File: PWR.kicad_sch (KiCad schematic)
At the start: 36 parts, among them J1 Conn_01x04_Pin, J10 Conn_01x02_Pin, J2 Conn_01x03_Pin, J3 Conn_01x03_Pin, J4 Conn_01x03_Pin, J5 Conn_01x03_Pin, U1 LM66100DCK, U2 XC6206P332MR, U4 MCP6001-OT

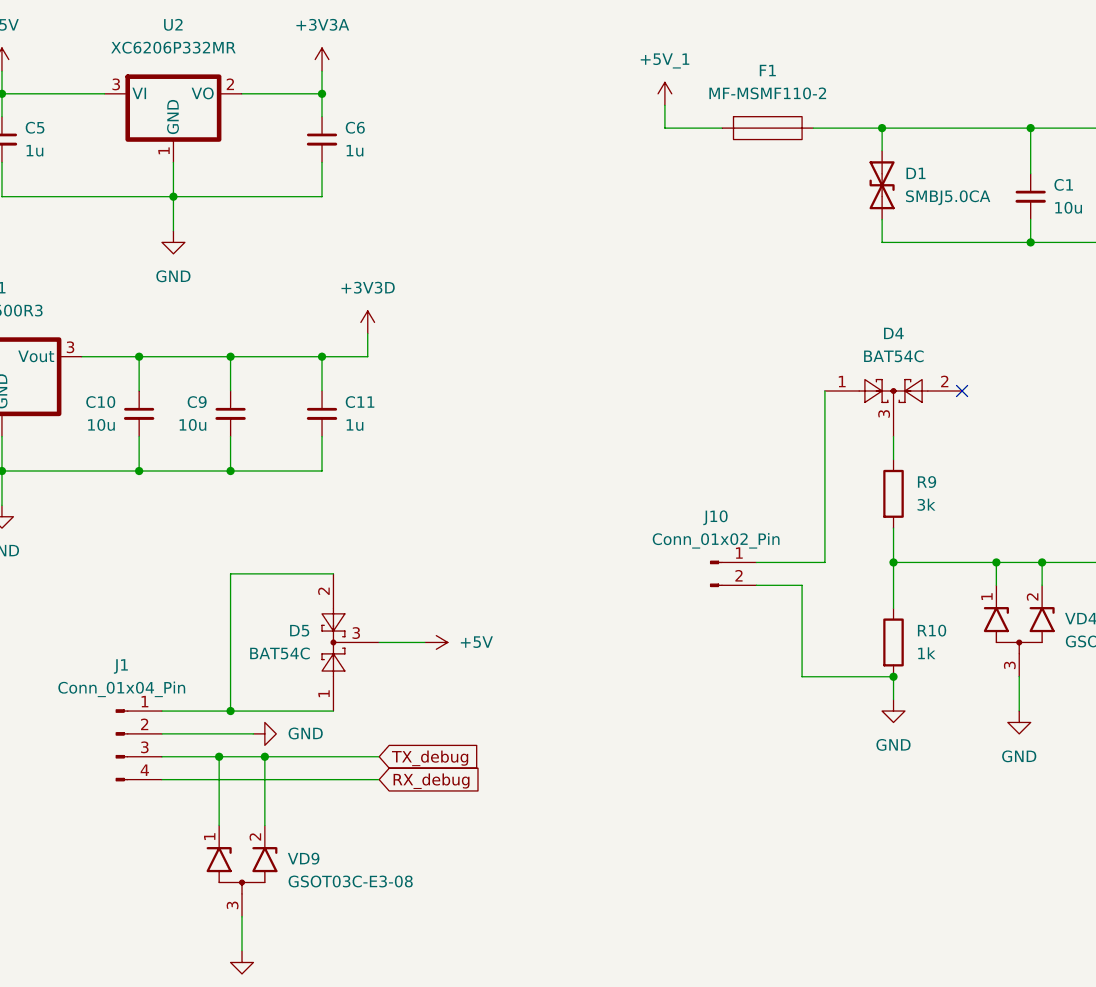
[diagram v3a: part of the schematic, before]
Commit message: feat: complete schematic, and start PCB
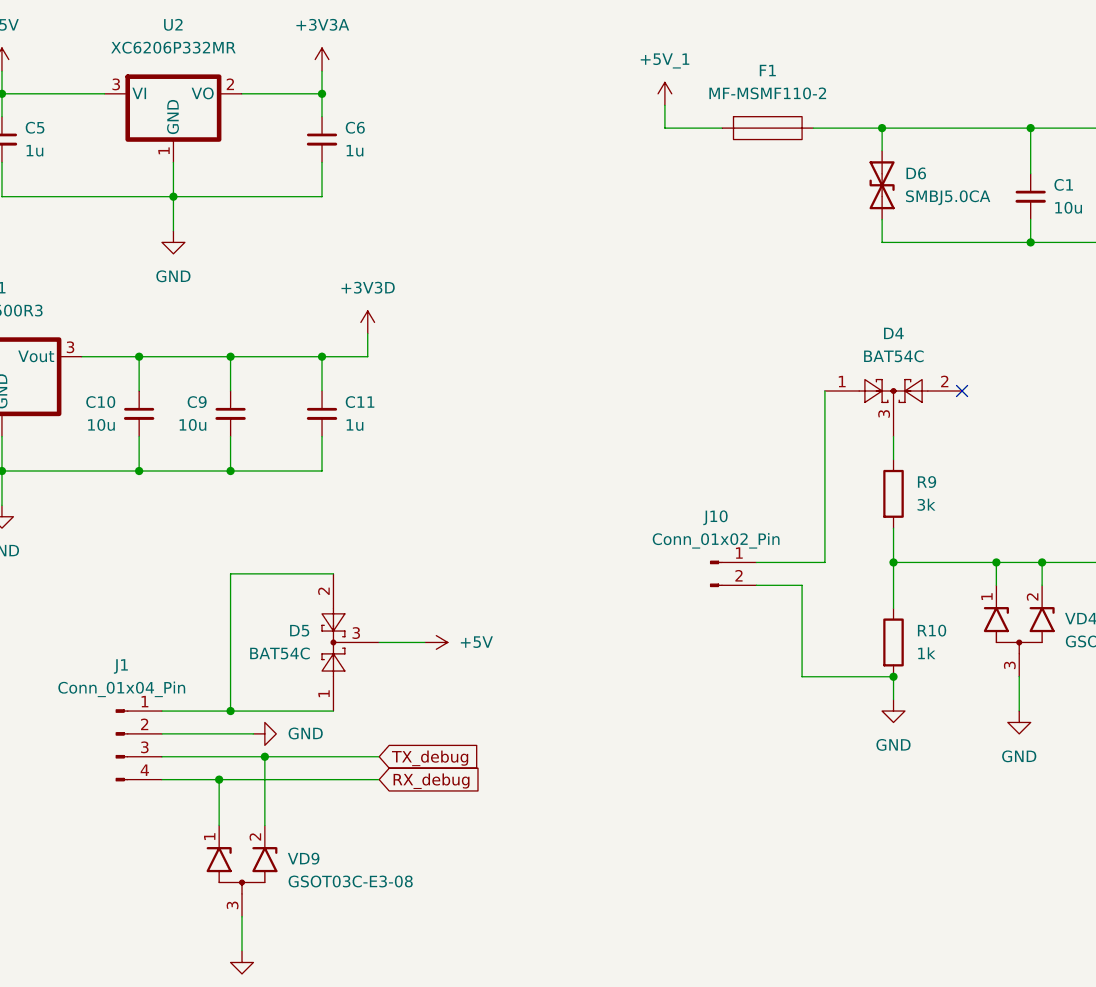
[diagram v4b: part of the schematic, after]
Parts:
- removed D1: SMBJ5.0CA, Diode_SMD:D_SMB_Handsoldering, symbol TVS:SMBJ5.0CA
- added D6: SMBJ5.0CA, Diode_SMD:D_SMB_Handsoldering, symbol TVS:SMBJ5.0CA
- C10, C11, C2, C3, C4, C5, C6, C7, C8, C9: footprint Capacitor_SMD:C_0805_2012Metric -> Capacitor_SMD:C_0805_2012Metric_Pad1.18x1.45mm_HandSolder
- U2: footprint Package_TO_SOT_SMD:SOT-23-3 -> Package_TO_SOT_SMD:SOT-23_Handsoldering
- U4: footprint Package_TO_SOT_SMD:SOT-23-5 -> Package_TO_SOT_SMD:SOT-23-5_HandSoldering
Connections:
- net +5V_1: now also F1.1 (A1); no longer F1.
- net GND: now also D6.1 (A1)
- net RX_debug: now also VD9.1 (K1)
- net TX_debug: no longer VD9.1 (K1)
- net at C1.1, C2.1, C3.1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: now also F1.2 (A2), D6.2 (A2); no longer F1.
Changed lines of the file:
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@@
 	)
 	(junction
+		(at 85.09 153.67)
+		(diameter 0)
+		(color 0 0 0 0)
+	)
+	(junction
 		(at 140.97 40.64)
 		(diameter 0)
@@
 	)
 	(junction
-		(at 85.09 151.13)
-		(diameter 0)
-		(color 0 0 0 0)
-	)
-	(junction
 		(at 199.39 129.54)
 		(diameter 0)
@@
 	(wire
 		(pts
-			(xy 85.09 151.13) (xy 90.17 151.13)
+			(xy 78.74 151.13) (xy 90.17 151.13)
 		)
 		(stroke
@@
 	(wire
 		(pts
-			(xy 78.74 151.13) (xy 85.09 151.13)
-		)
-		(stroke
-			(width 0)
-			(type default)
-		)
-	)
-	(wire
-		(pts
 			(xy 201.93 81.28) (xy 201.93 86.36)
 		)
@@
 	(wire
 		(pts
-			(xy 78.74 153.67) (xy 102.87 153.67)
+			(xy 78.74 153.67) (xy 85.09 153.67)
 		)
 		(stroke
@@
 	(wire
 		(pts
-			(xy 85.09 151.13) (xy 85.09 158.75)
+			(xy 85.09 153.67) (xy 102.87 153.67)
 		)
 		(stroke
@@
 	(wire
 		(pts
+			(xy 85.09 153.67) (xy 85.09 158.75)
+		)
+		(stroke
+			(width 0)
+			(type default)
+		)
+	)
+	(wire
+		(pts
 			(xy 111.76 35.56) (xy 95.25 35.56)
 		)
@@
 			)
 		)
-		(property "Footprint" "Package_TO_SOT_SMD:SOT-23-5"
+		(property "Footprint" "Package_TO_SOT_SMD:SOT-23-5_HandSoldering"
 			(at 218.44 137.16 0)
 			(hide yes)
@@
 			)
 		)
-		(property "Footprint" "Capacitor_SMD:C_0805_2012Metric"
+		(property "Footprint" "Capacitor_SMD:C_0805_2012Metric_Pad1.18x1.45mm_HandSolder"
 			(at 201.93 88.9 0)
 			(hide yes)
@@
 			)
 		)
-		(property "Footprint" "Capacitor_SMD:C_0805_2012Metric"
+		(property "Footprint" "Capacitor_SMD:C_0805_2012Metric_Pad1.18x1.45mm_HandSolder"
 			(at 45.72 113.03 0)
 			(hide yes)
@@
 			)
 		)
-		(property "Footprint" "Capacitor_SMD:C_0805_2012Metric"
+		(property "Footprint" "Capacitor_SMD:C_0805_2012Metric_Pad1.18x1.45mm_HandSolder"
 			(at 76.2 113.03 0)
 			(hide yes)
@@
 	)
 	(symbol
+		(lib_name "SMBJ5.0CA_1")
+		(lib_id "TVS:SMBJ5.0CA")
+		(at 158.75 87.63 90)
+		(unit 1)
+		(body_style 1)
+		(exclude_from_sim no)
+		(in_bom yes)
+		(on_board yes)
+		(in_pos_files yes)
+		(dnp no)
+		(fields_autoplaced yes)
+		(property "Reference" "D6"
+			(at 161.29 86.3599 90)
+			(show_name no)
+			(do_not_autoplace no)
+			(effects
+				(font
+					(size 1.27 1.27)
+				)
+				(justify right)
+			)
+		)
+		(property "Value" "SMBJ5.0CA"
+			(at 161.29 88.8999 90)
+			(show_name no)
+			(do_not_autoplace no)
+			(effects
+				(font
+					(size 1.27 1.27)
+				)
+				(justify right)
+			)
+		)
+		(property "Footprint" "Diode_SMD:D_SMB_Handsoldering"
+			(at 163.83 87.63 0)
+			(hide yes)
+			(show_name no)
+			(do_not_autoplace no)
+			(effects
+				(font
+					(size 1.27 1.27)
+				)
+			)
+		)
+		(property "Datasheet" "https://static.chipdip.ru/lib/863/DOC025863762.pdf"
+			(at 172.466 89.662 0)
+			(hide yes)
+			(show_name no)
+			(do_not_autoplace no)
+			(effects
+				(font
+					(size 1.27 1.27)
+				)
+			)
+		)
+		(property "Description" "TVS 600Вт 5В двунаправленный"
+			(at 169.164 92.202 0)
+			(hide yes)
+			(show_name no)
+			(do_not_autoplace no)
+			(effects
+				(font
+					(size 1.27 1.27)
+				)
+			)
+		)
+		(pin "1"
+		)
+		(pin "2"
+		)
+		(instances
+			(project "Magister_work_v1"
+				(path "/9ff4e5e8-ab59-4c4d-a10a-f8f5e444c5cb/6e6c00e0-c4a8-403b-83b3-c44ac9f0fdda"
+					(reference "D6")
+					(unit 1)
+				)
+			)
+		)
+	)
+	(symbol
 		(lib_id "Device:R")
 		(at 160.02 121.92 0)
@@
 			)
 		)
-		(property "Footprint" "Capacitor_SMD:C_0805_2012Metric"
+		(property "Footprint" "Capacitor_SMD:C_0805_2012Metric_Pad1.18x1.45mm_HandSolder"
 			(at 248.92 85.09 0)
 			(hide yes)
@@
 			)
 		)
-		(property "Footprint" "Capacitor_SMD:C_0805_2012Metric"
+		(property "Footprint" "Capacitor_SMD:C_0805_2012Metric_Pad1.18x1.45mm_HandSolder"
 			(at 96.52 82.55 0)
 			(hide yes)
@@
 			)
 		)
-		(property "Footprint" "Package_TO_SOT_SMD:SOT-23-3"
+		(property "Footprint" "Package_TO_SOT_SMD:SOT-23_Handsoldering"
 			(at 81.28 67.056 0)
 			(hide yes)
@@
 			)
 		)
-		(property "Footprint" "Capacitor_SMD:C_0805_2012Metric"
+		(property "Footprint" "Capacitor_SMD:C_0805_2012Metric_Pad1.18x1.45mm_HandSolder"
 			(at 60.96 82.55 0)
 			(hide yes)
@@
 			)
 		)
-		(property "Footprint" "Capacitor_SMD:C_0805_2012Metric"
+		(property "Footprint" "Capacitor_SMD:C_0805_2012Metric_Pad1.18x1.45mm_HandSolder"
 			(at 96.52 113.03 0)
 			(hide yes)
@@
 			)
 		)
-		(property "Footprint" "Capacitor_SMD:C_0805_2012Metric"
+		(property "Footprint" "Capacitor_SMD:C_0805_2012Metric_Pad1.18x1.45mm_HandSolder"
 			(at 86.36 113.03 0)
 			(hide yes)
@@
 			)
 		)
-		(property "Footprint" "Capacitor_SMD:C_0805_2012Metric"
+		(property "Footprint" "Capacitor_SMD:C_0805_2012Metric_Pad1.18x1.45mm_HandSolder"
 			(at 190.5 88.9 0)
 			(hide yes)
@@
 			)
 		)
-		(property "Footprint" "Capacitor_SMD:C_0805_2012Metric"
+		(property "Footprint" "Capacitor_SMD:C_0805_2012Metric_Pad1.18x1.45mm_HandSolder"
 			(at 34.29 113.03 0)
 			(hide yes)
@@
 	)
 	(symbol
-		(lib_id "TVS:SMBJ5.0CA")
-		(at 158.75 87.63 90)
-		(unit 1)
-		(body_style 1)
-		(exclude_from_sim no)
-		(in_bom yes)
-		(on_board yes)
-		(in_pos_files yes)
-		(dnp no)
-		(fields_autoplaced yes)
-		(property "Reference" "D1"
-			(at 161.29 86.3599 90)
-			(show_name no)
-			(do_not_autoplace no)
-			(effects
-				(font
-					(size 1.27 1.27)
-				)
-				(justify right)
-			)
-		)
-		(property "Value" "SMBJ5.0CA"
-			(at 161.29 88.8999 90)
-			(show_name no)
-			(do_not_autoplace no)
-			(effects
-				(font
-					(size 1.27 1.27)
-				)
-				(justify right)
-			)
-		)
-		(property "Footprint" "Diode_SMD:D_SMB_Handsoldering"
-			(at 163.83 87.63 0)
-			(hide yes)
-			(show_name no)
-			(do_not_autoplace no)
-			(effects
-				(font
-					(size 1.27 1.27)
-				)
-			)
-		)
-		(property "Datasheet" "https://static.chipdip.ru/lib/863/DOC025863762.pdf"
-			(at 172.466 89.662 0)
-			(hide yes)
-			(show_name no)
-			(do_not_autoplace no)
-			(effects
-				(font
-					(size 1.27 1.27)
-				)
-			)
-		)
-		(property "Description" "Защитный диод двунаправленный 600Вт 5В"
-			(at 169.164 92.202 0)
-			(hide yes)
-			(show_name no)
-			(do_not_autoplace no)
-			(effects
-				(font
-					(size 1.27 1.27)
-				)
-			)
-		)
-		(pin "2"
-		)
-		(pin "1"
-		)
-		(instances
-			(project "Magister_work_v1"
-				(path "/9ff4e5e8-ab59-4c4d-a10a-f8f5e444c5cb/6e6c00e0-c4a8-403b-83b3-c44ac9f0fdda"
-					(reference "D1")
-					(unit 1)
-				)
-			)
-		)
-	)
-	(symbol
 		(lib_id "power:+5V")
 		(at 149.86 38.1 270)
@@
 	)
 	(symbol
-		(lib_id "FUSE:MF-MSMF110-2")
-		(at 146.05 81.28 0)
+		(lib_id "power:+5V")
+		(at 96.52 74.93 0)
 		(unit 1)
 		(body_style 1)
@@
 		(dnp no)
 		(fields_autoplaced yes)
-		(property "Reference" "F1"
-			(at 146.05 74.93 0)
+		(property "Reference" "#PWR021"
+			(at 96.52 78.74 0)
+			(hide yes)
 			(show_name no)
 			(do_not_autoplace no)
@@
 			)
 		)
-		(property "Value" "MF-MSMF110-2"
-			(at 146.05 77.47 0)
+		(property "Value" "+3V3A"
+			(at 96.52 69.85 0)
 			(show_name no)
 			(do_not_autoplace no)
@@
 			)
 		)
-		(property "Footprint" "Fuse:Fuse_1812_4532Metric_Pad1.30x3.40mm_HandSolder"
-			(at 145.288 91.44 0)
+		(property "Footprint" ""
+			(at 96.52 74.93 0)
 			(hide yes)
 			(show_name no)
@@
 		)
 		(property "Datasheet" ""
-			(at 146.05 81.28 0)
+			(at 96.52 74.93 0)
 			(hide yes)
 			(show_name no)
@@
 			)
 		)
-		(property "Description" "MF-MSMF110-2, 1.1А, 1812, Предохранитель самовосстанавливающийся, MultiFuse SMD"
-			(at 144.526 86.868 0)
+		(property "Description" "Power symbol creates a global label with name \"+5V\""
+			(at 96.52 74.93 0)
 			(hide yes)
 			(show_name no)
@@
 			)
 		)
-		(pin ""
-		)
-		(pin ""
+		(pin "1"
 		)
 		(instances
 			(project "Magister_work_v1"
 				(path "/9ff4e5e8-ab59-4c4d-a10a-f8f5e444c5cb/6e6c00e0-c4a8-403b-83b3-c44ac9f0fdda"
-					(reference "F1")
+					(reference "#PWR021")
 					(unit 1)
 				)
@@
 	)
 	(symbol
-		(lib_id "power:+5V")
-		(at 96.52 74.93 0)
+		(lib_id "FUSE:MF-MSMF110-2")
+		(at 146.05 81.28 0)
 		(unit 1)
 		(body_style 1)
@@
 		(dnp no)
 		(fields_autoplaced yes)
-		(property "Reference" "#PWR021"
-			(at 96.52 78.74 0)
-			(hide yes)
+		(property "Reference" "F1"
+			(at 146.05 74.93 0)
 			(show_name no)
 			(do_not_autoplace no)
@@
 			)
 		)
-		(property "Value" "+3V3A"
-			(at 96.52 69.85 0)
+		(property "Value" "MF-MSMF110-2"
+			(at 146.05 77.47 0)
 			(show_name no)
 			(do_not_autoplace no)
@@
 			)
 		)
-		(property "Footprint" ""
-			(at 96.52 74.93 0)
+		(property "Footprint" "Fuse:Fuse_1812_4532Metric_Pad1.30x3.40mm_HandSolder"
+			(at 145.288 91.44 0)
 			(hide yes)
 			(show_name no)
@@
 		)
 		(property "Datasheet" ""
-			(at 96.52 74.93 0)
+			(at 146.05 81.28 0)
 			(hide yes)
 			(show_name no)
@@
 			)
 		)
-		(property "Description" "Power symbol creates a global label with name \"+5V\""
-			(at 96.52 74.93 0)
+		(property "Description" "MF-MSMF110-2, 1.1А, 1812, Предохранитель самовосстанавливающийся, MultiFuse SMD"
+			(at 144.526 86.868 0)
 			(hide yes)
 			(show_name no)
@@
 			)
 		)
+		(pin "2"
+		)
 		(pin "1"
 		)
@@
 			(project "Magister_work_v1"
 				(path "/9ff4e5e8-ab59-4c4d-a10a-f8f5e444c5cb/6e6c00e0-c4a8-403b-83b3-c44ac9f0fdda"
-					(reference "#PWR021")
+					(reference "F1")
 					(unit 1)
 				)

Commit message: feat: start PCB trace
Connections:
- net at R10.1, R11.1, R9.2: no longer VD4.1 (K1), VD4.2 (K2)
- net at C29.1, R11.2, U4.3 (+): now also VD4.1 (K1), VD4.2 (K2)
- net +5V_2: now reaches C1.1, C2.1, C3.1, D6.2 (A2), F1.2 (A2), U1.1 (VIN)
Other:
- moved on the sheet: R11, VD4
